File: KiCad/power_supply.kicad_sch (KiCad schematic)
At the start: 16 parts, among them SW1 SW_Push, U1 STM32F401RBTx

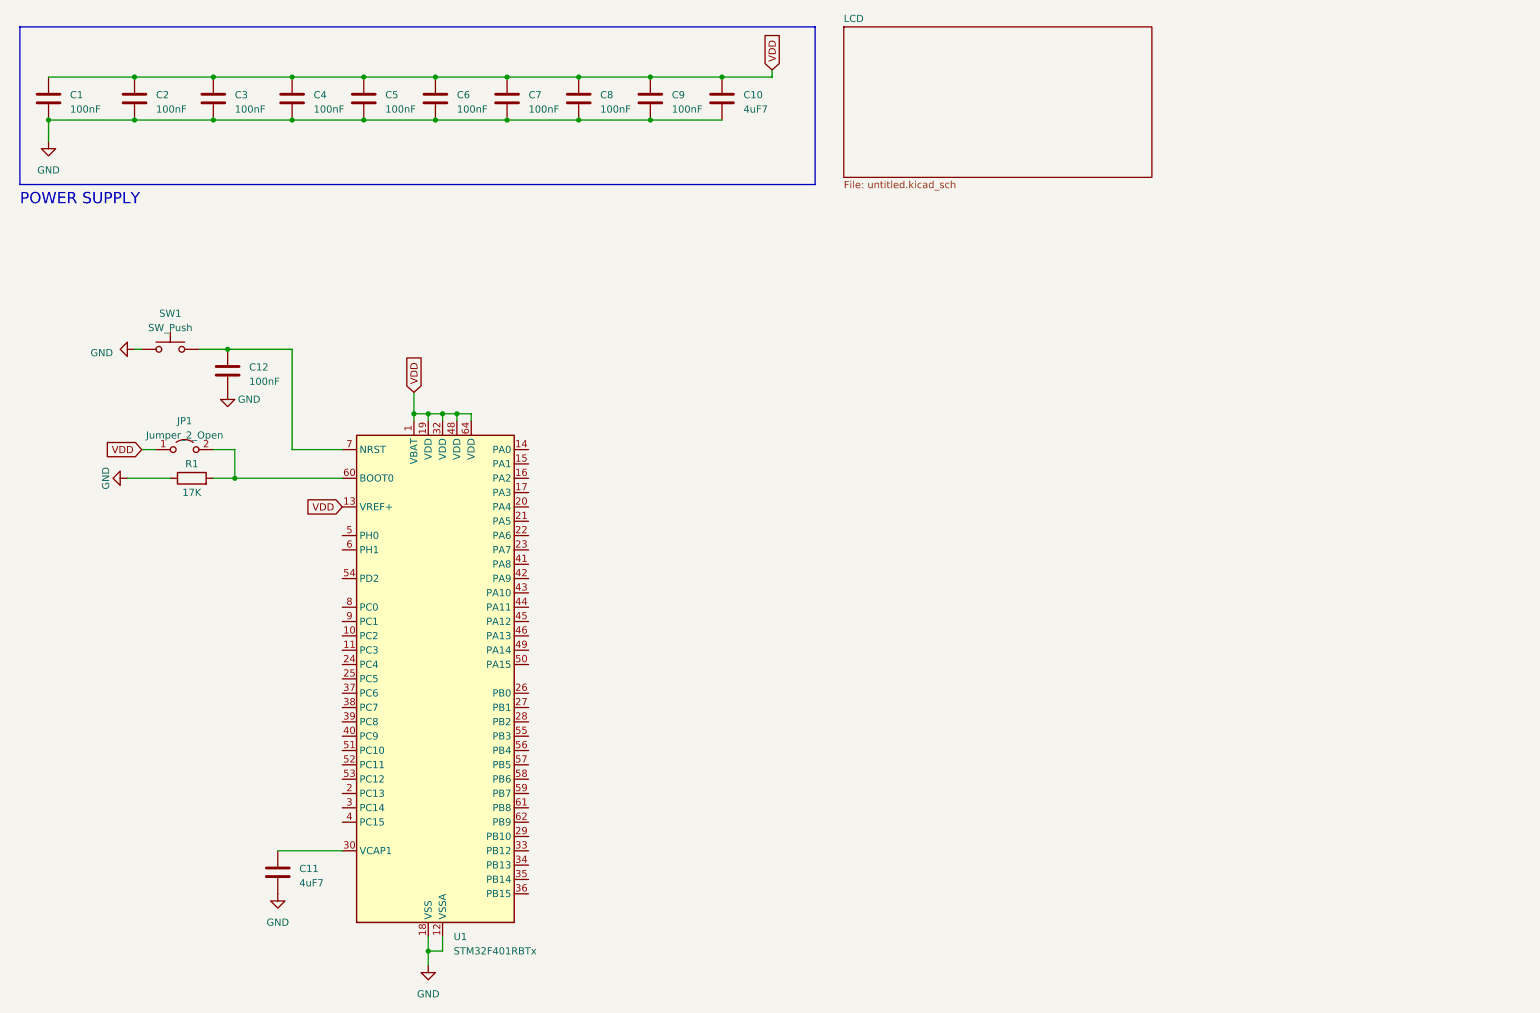
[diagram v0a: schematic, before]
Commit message: added power schematic to design
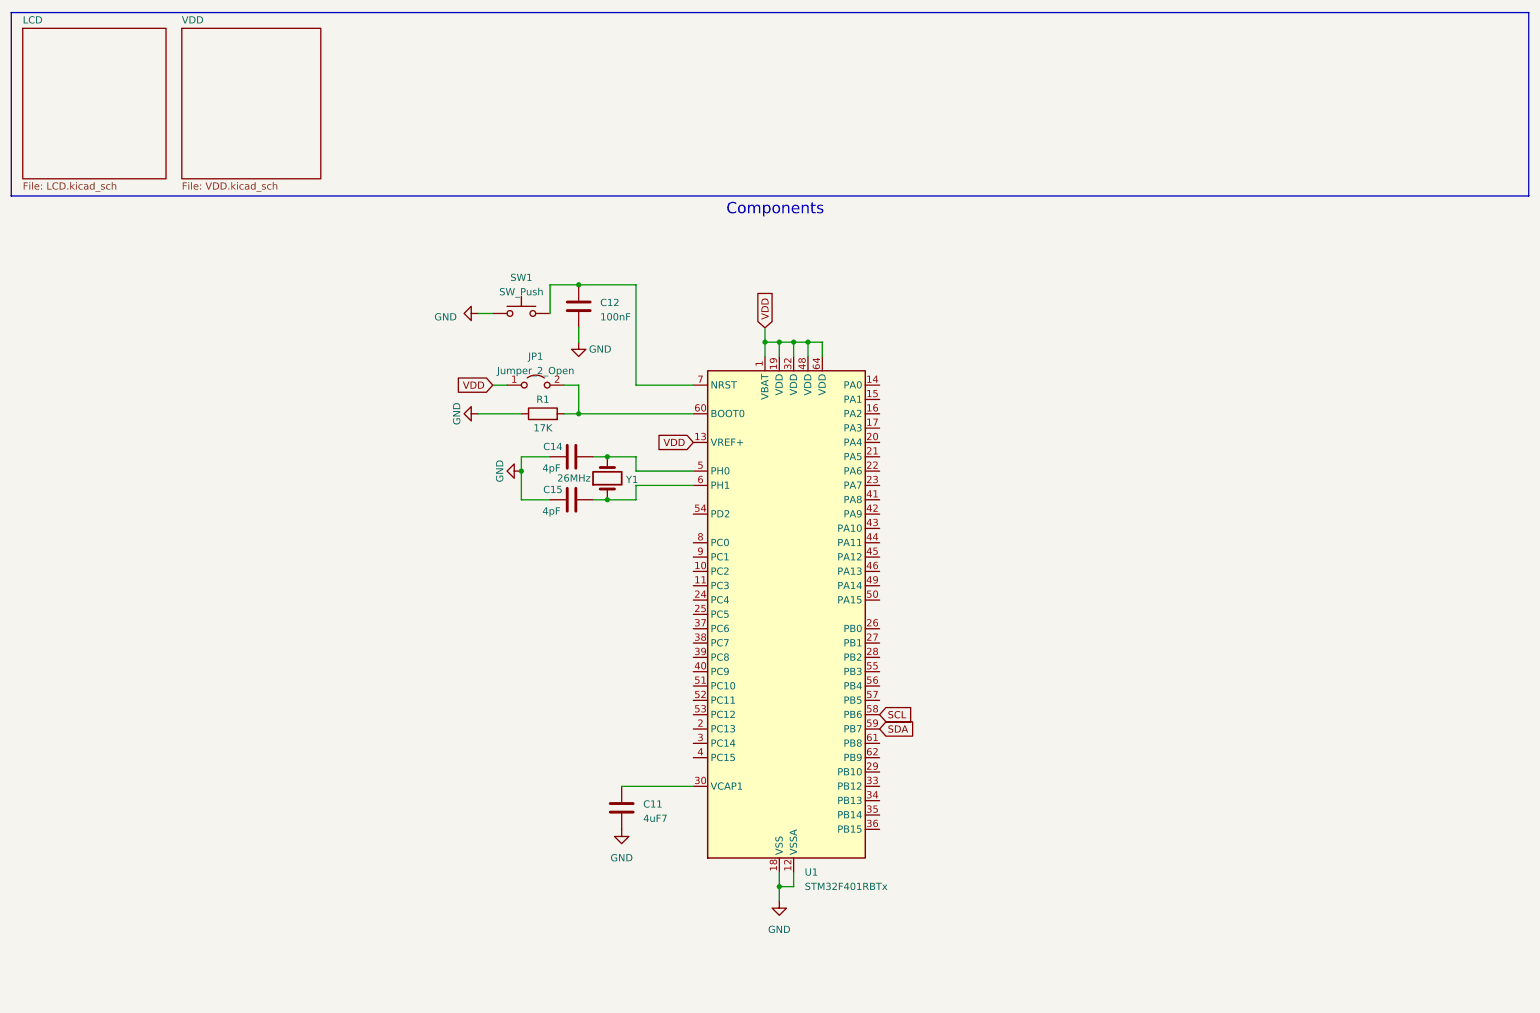
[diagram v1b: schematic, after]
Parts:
- removed C1, C2, C3, C4, C5, C6, C7, C8, C9: 100nF, symbol Device:C
- removed C10: 4uF7, symbol Device:C
- added C14, C15: 4pF, symbol Device:C
- added Y1: 26MHz, symbol Device:Crystal
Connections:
- net GND: now also C14.1, C15.1
- net at U1.5 (PH0): now also C14.2, Y1.2
- net SCL: now reaches U1.58 (PB6)
- net SDA: now reaches U1.59 (PB7)
- net at U1.6 (PH1): now also C15.2, Y1.1
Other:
- added sheet VDD (VDD.kicad_sch)
- sheet LCD: file untitled.kicad_sch -> LCD.kicad_sch
- note added: "Components"
- note removed: "POWER SUPPLY"
- moved on the sheet: C11, C12, JP1, R1, SW1, U1
